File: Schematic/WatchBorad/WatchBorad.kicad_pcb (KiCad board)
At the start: 4 copper layers, 35 x 35 mm, 118 parts, among them J1 Conn_01x07_Female, J3 TYPE-C-31-M-17, M1 Motor_DC, SW1 SW_Push, SW2 SW_Push, SW3 SW_Push, SW4 SW_Push, SW5 SW_Push, U1 LSM6DSLTR, U10 TPS62740DSST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

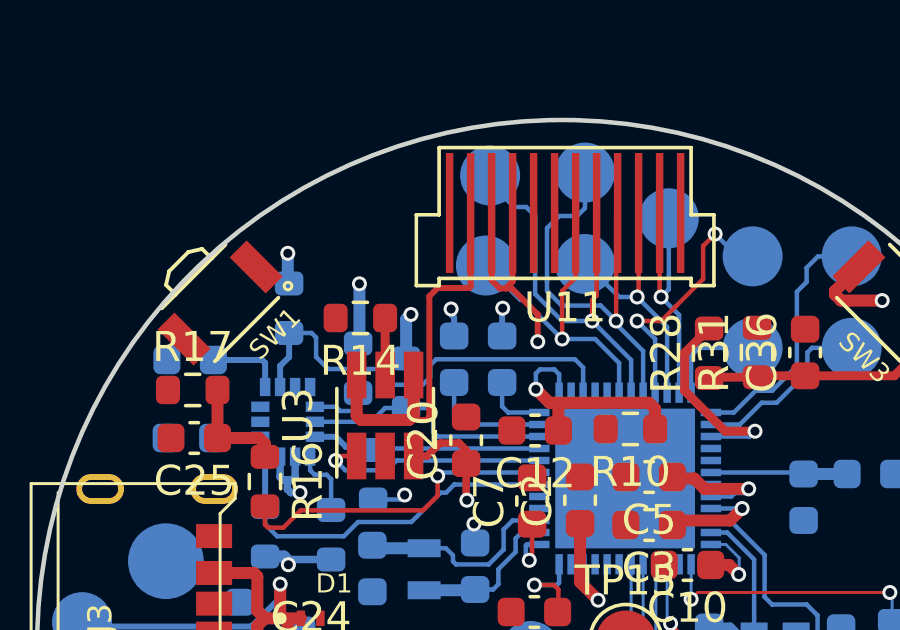
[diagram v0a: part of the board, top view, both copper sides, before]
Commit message: Added display's GND via
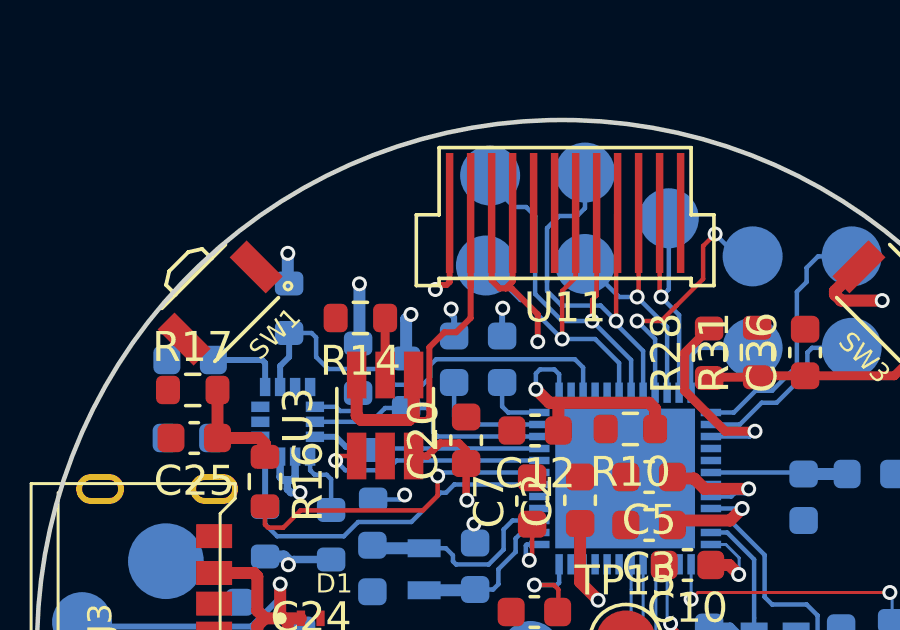
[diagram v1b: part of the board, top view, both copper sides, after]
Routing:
- net GND: track 7.57 -> 10.4 mm, vias 5 -> 6

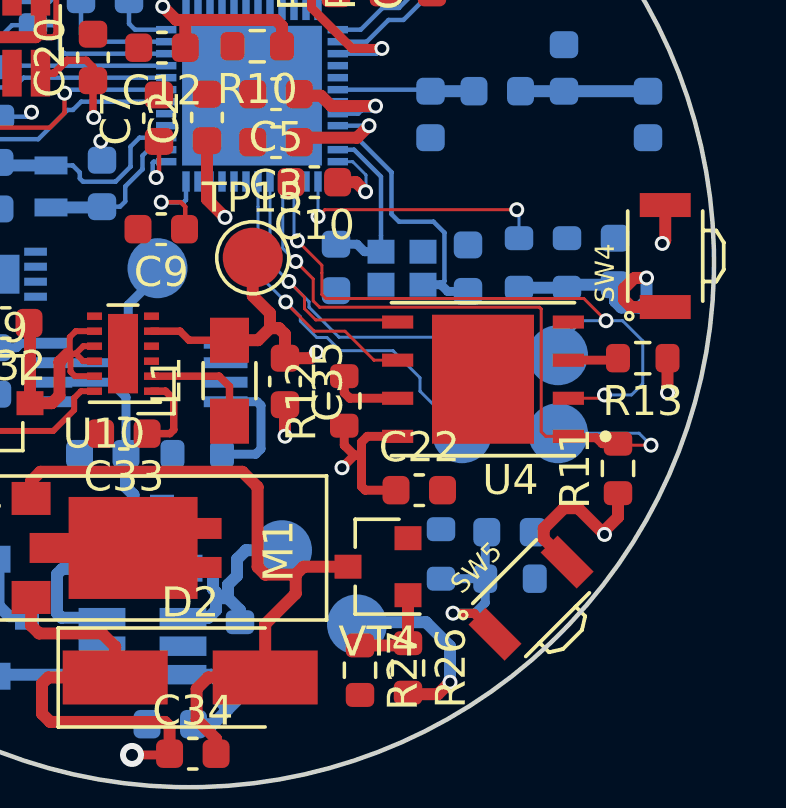
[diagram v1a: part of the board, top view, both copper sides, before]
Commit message: Fixed DRC warnings
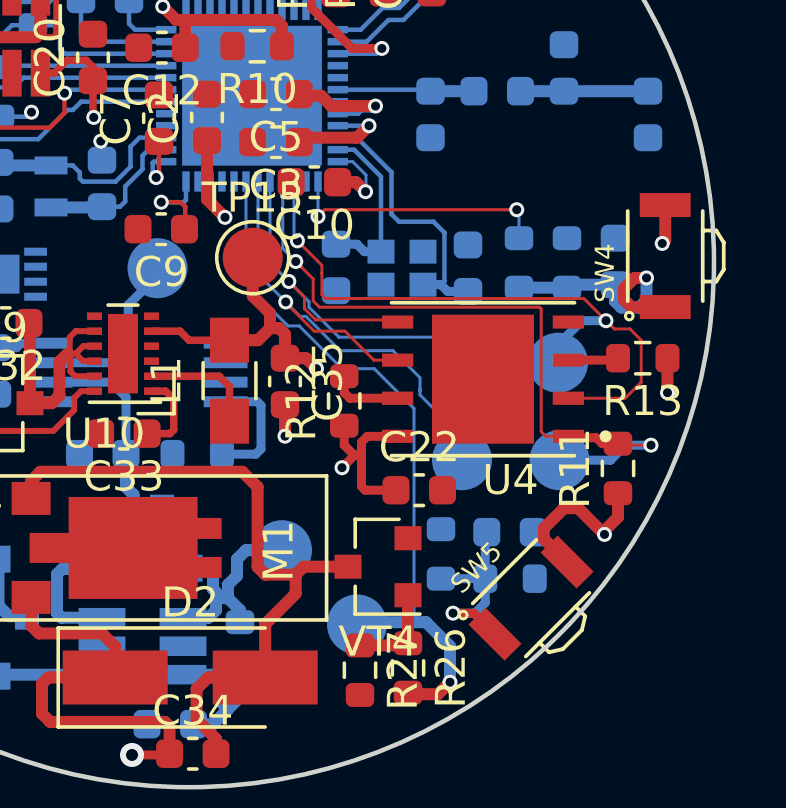
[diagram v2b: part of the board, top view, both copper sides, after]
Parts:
- moved TP17 0.90 mm to (101.2, 95.5)
- moved TP19 0.90 mm to (98.0, 95.5)
- moved TP16 0.25 mm to (101.2, 92.2)
- moved TP18 0.25 mm to (98.0, 92.2)
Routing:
- net /DCDC&PB/Enable_motor: track 6.25 -> 24.1 mm
- net /MCU/FLASH_SCK: track 17.0 -> 18.1 mm
- net /MCU/FLASH_MISO: track 22.7 -> 23.5 mm, vias 3 -> 2

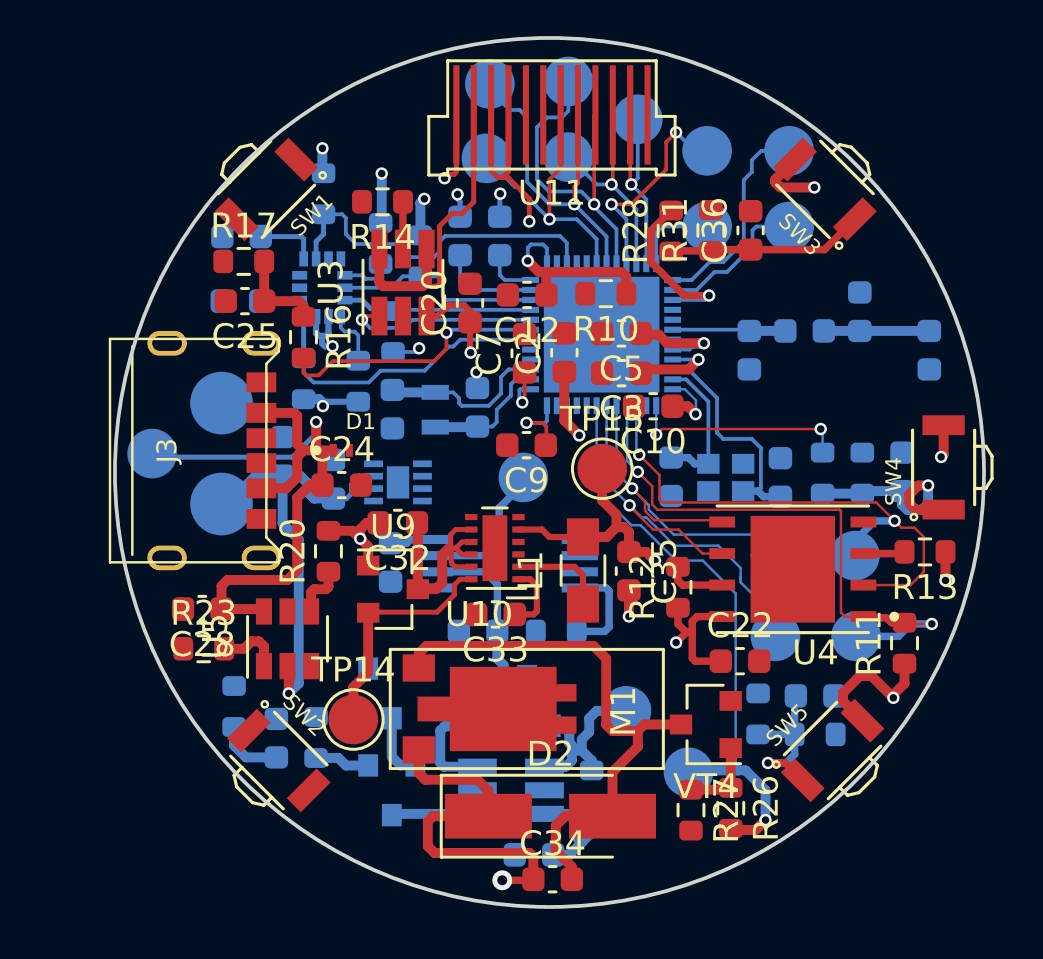
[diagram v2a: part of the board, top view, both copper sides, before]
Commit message: Added GND plane routing
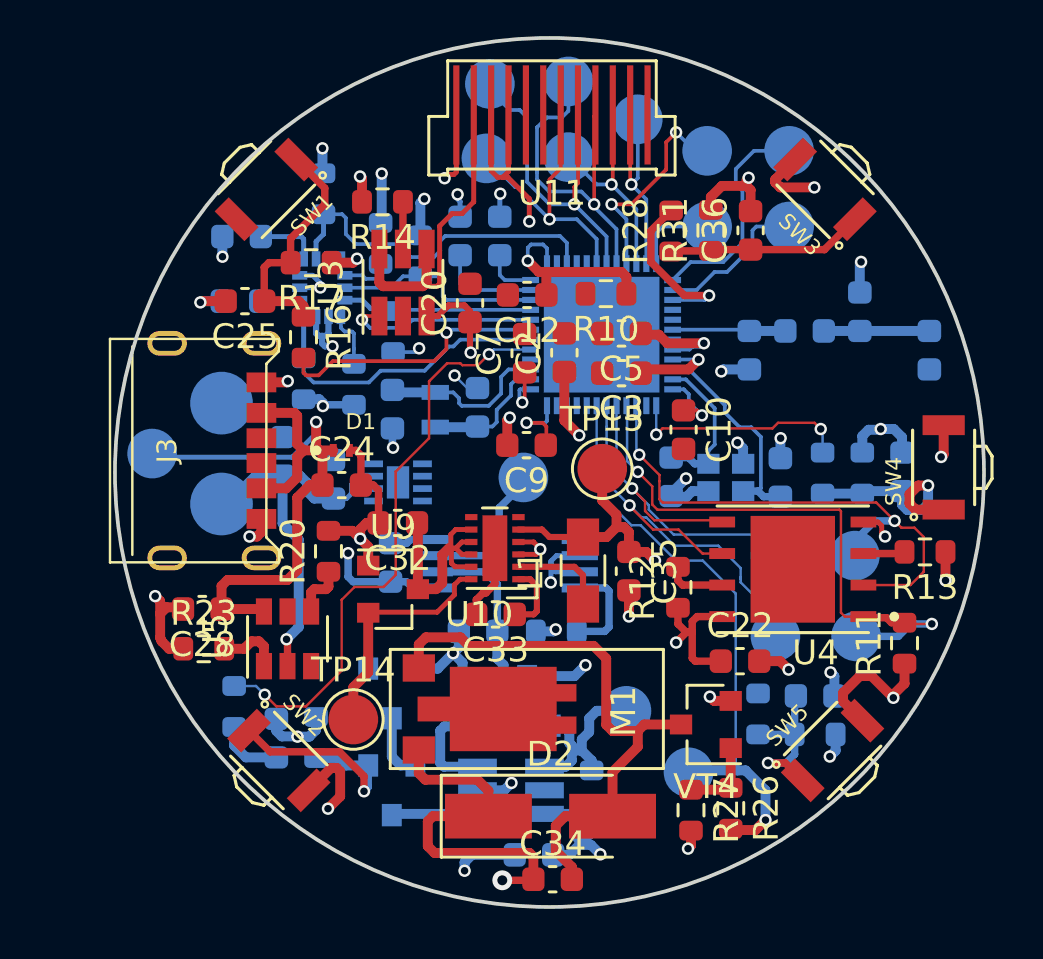
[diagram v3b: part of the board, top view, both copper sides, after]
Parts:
- moved R17 2.71 mm to (79.3, 80.5), turned to 180 degrees
- moved C10 1.54 mm to (94.3, 87.2), turned to 270 degrees
- moved R5 0.22 mm to (81.0, 85.3)
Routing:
- net GND: track 10.4 -> 74.5 mm, vias 6 -> 37
- net +BATT: track 24.2 -> 55.4 mm, vias 1 -> 4
- net /MCU/PB_1_MCU: track 0.00 -> 23.7 mm, vias 0 -> 2
- net Net-(C26-Pad1): track 4.87 -> 12.0 mm, vias 0 -> 1
- net Net-(C25-Pad1): track 3.77 -> 9.87 mm
- net /MCU/XC2: track 6.62 -> 7.18 mm
- net Net-(C34-Pad2): track 23.1 -> 23.6 mm

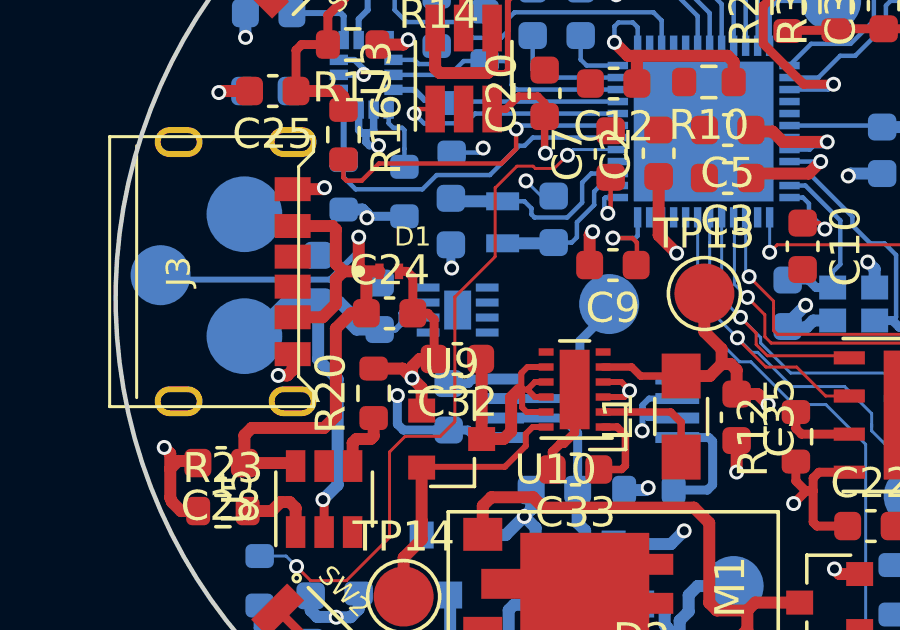
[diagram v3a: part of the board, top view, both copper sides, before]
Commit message: Added GND plane routing
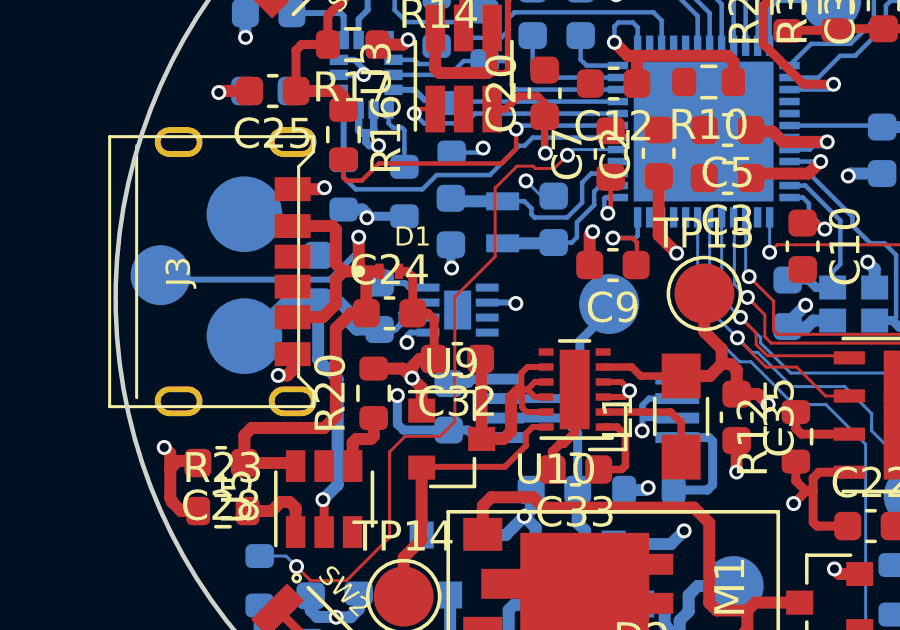
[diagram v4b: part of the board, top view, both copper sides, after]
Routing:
- net GND: track 74.5 -> 78.1 mm, vias 37 -> 39

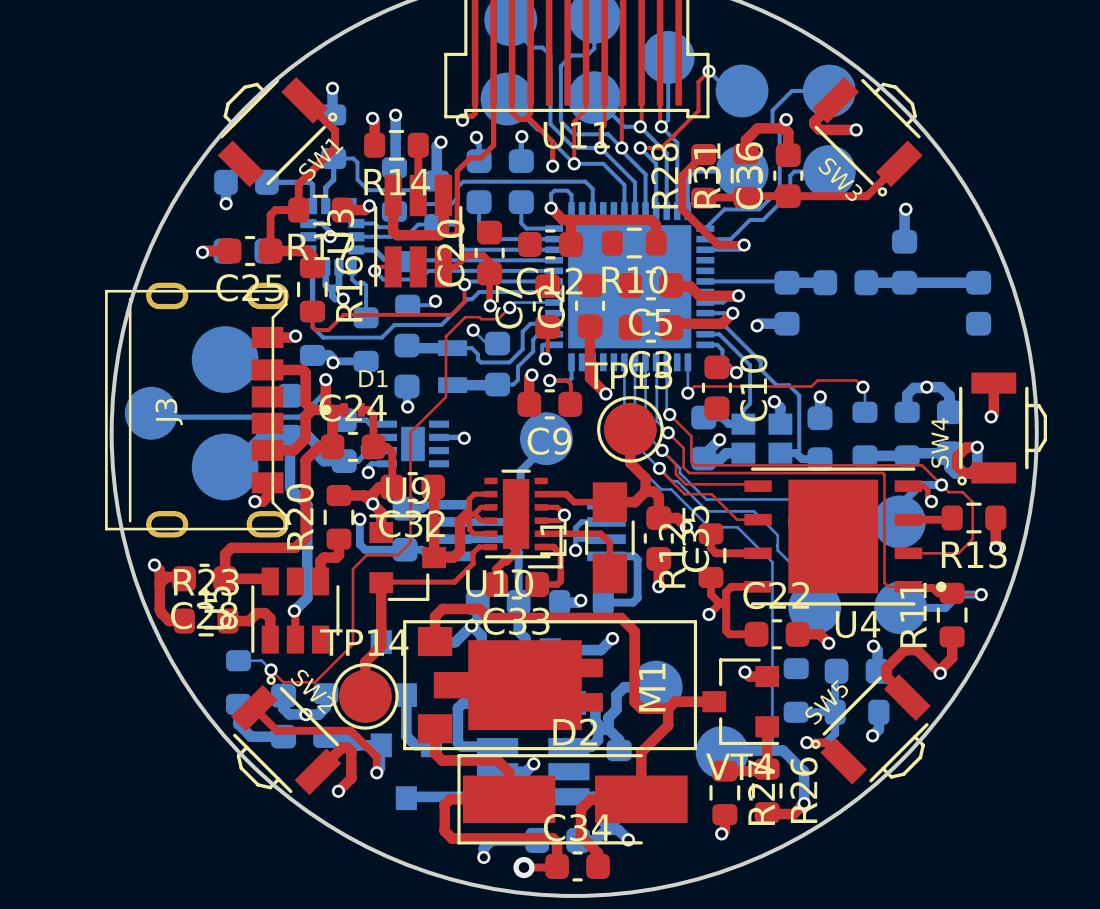
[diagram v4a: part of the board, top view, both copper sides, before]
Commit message: Added PCB route for GND vias
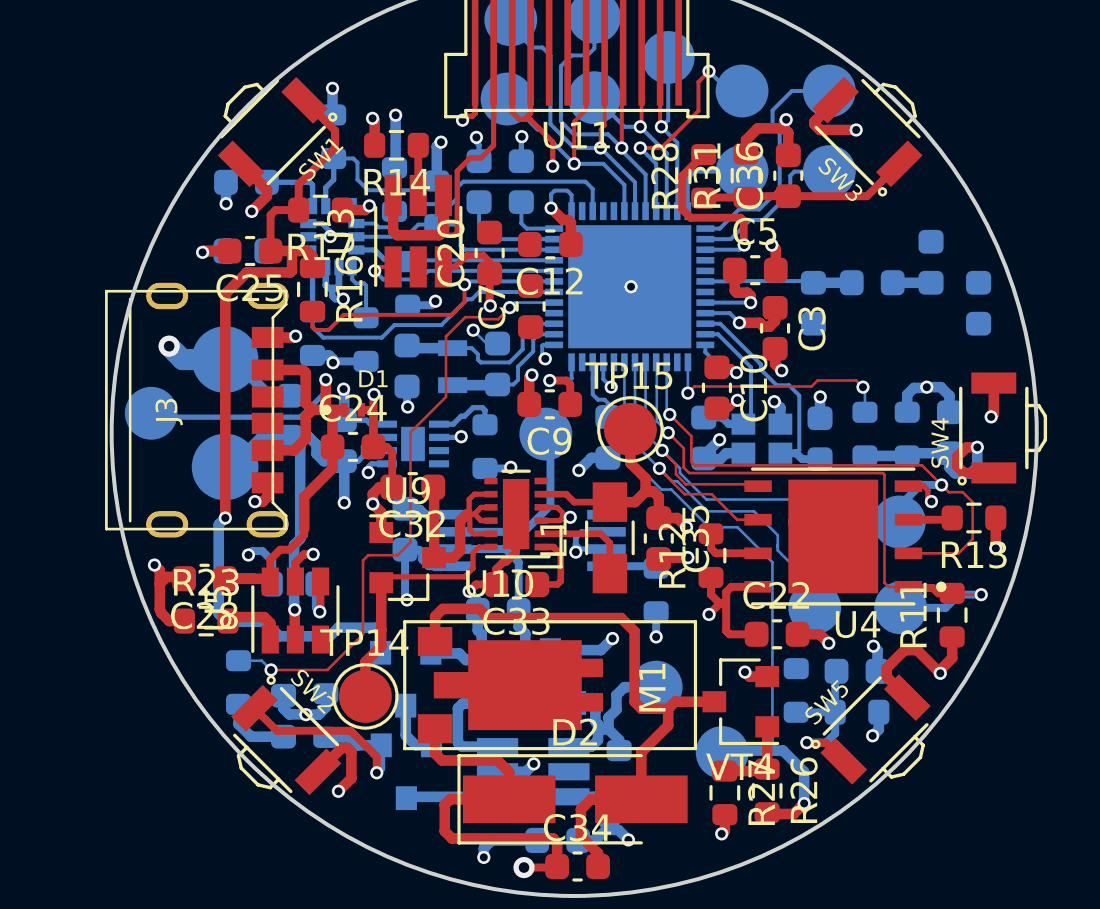
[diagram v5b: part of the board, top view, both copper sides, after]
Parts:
- C2, R10, R20: moved to B.Cu
- moved R10 9.55 mm to (85.5, 89.4), turned to 90 degrees
- moved C2 5.02 mm to (90.2, 89.0), turned to 270 degrees
- moved C3 4.70 mm to (96.5, 84.9), turned to 270 degrees
- moved C5 3.99 mm to (95.8, 82.7), turned to 0 degrees
- moved R20 3.04 mm to (78.3, 94.6), turned to 180 degrees
- moved R24 2.86 mm to (92.0, 94.8), turned to 270 degrees
- moved 3.9nH1 1.00 mm to (100.2, 83.2)
- moved C13 1.00 mm to (102.4, 82.4)
- moved C15 1.00 mm to (98.0, 84.0)
- moved C7 0.65 mm to (87.2, 84.1)
- moved VT2 0.40 mm to (82.5, 98.2)
- moved U8 0.38 mm to (87.2, 92.9)
- moved C31 0.30 mm to (86.0, 95.6)
- moved TP12 0.18 mm to (87.8, 88.9)
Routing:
- net Net-(C25-Pad1): track 9.87 -> 33.2 mm, vias 0 -> 1
- net +BATT: track 55.4 -> 73.4 mm, vias 4 -> 6
- net GND: track 78.1 -> 92.6 mm, vias 39 -> 48
- net Net-(3.9nH1-Pad1): track 4.25 -> 1.45 mm
- net +3V3: track 183.4 -> 180.8 mm, vias 18 -> 19
- net /MCU/FG_OD_ALRT_N: track 0.00 -> 2.59 mm
- net /PSU_logic/Rlim: track 4.25 -> 1.91 mm
- net /MCU/DEC4: track 4.21 -> 2.58 mm, vias 1 -> 0
- net /MCU/DEC1: track 2.49 -> 1.20 mm
- net /DCDC&PB/DCDC_VIN: track 18.7 -> 19.9 mm
- net Net-(3.9nH1-Pad2): track 4.56 -> 5.57 mm
- net +5V: track 29.2 -> 28.2 mm
- net /MCU/DEC2: track 4.02 -> 3.42 mm
- net /MCU/PB_3_MCU: track 6.86 -> 7.39 mm
- net Net-(R20-Pad1): track 2.17 -> 2.27 mm, vias 0 -> 1
